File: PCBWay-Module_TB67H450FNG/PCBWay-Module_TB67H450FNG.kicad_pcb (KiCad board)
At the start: 2 copper layers, 16.3 x 19 mm, 6 parts, among them IC1 Motor_A, IC2 Motor_B, J1 Conn_01x07_Pin, J2 Conn_01x07_Pin

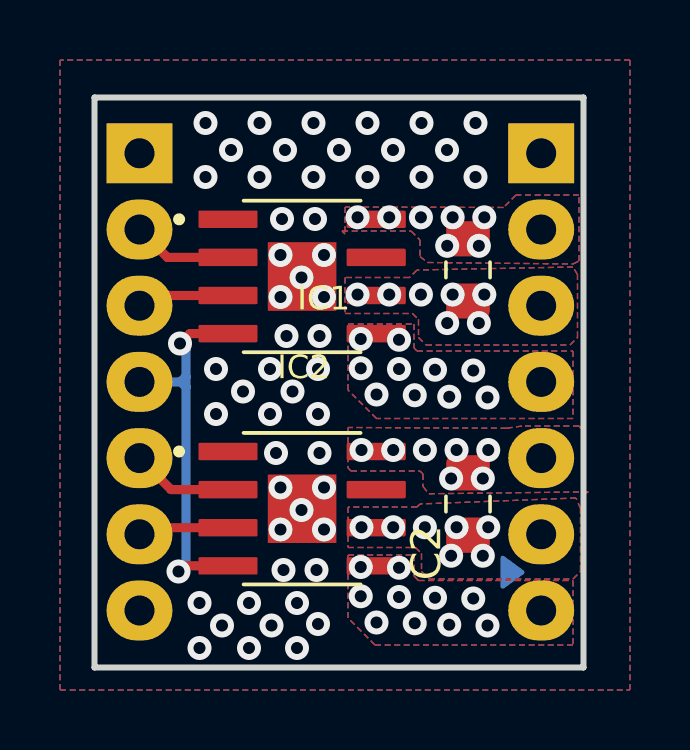
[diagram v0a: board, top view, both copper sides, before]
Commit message: Removed capacitors & update README.md
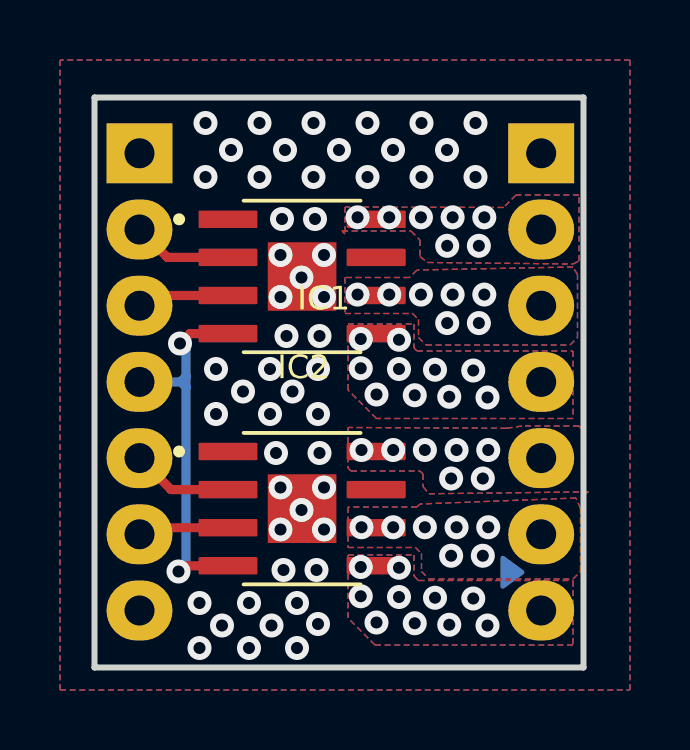
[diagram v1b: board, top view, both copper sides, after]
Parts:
- removed C2, C4: 100nF, Capacitor_SMD:C_0805_2012Metric_Pad1.18x1.45mm_HandSolder
